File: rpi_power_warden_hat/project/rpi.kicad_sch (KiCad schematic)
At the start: 5 parts, among them J1 Conn_01x06, J4 Conn_01x06, J5 Raspberry_Pi_4

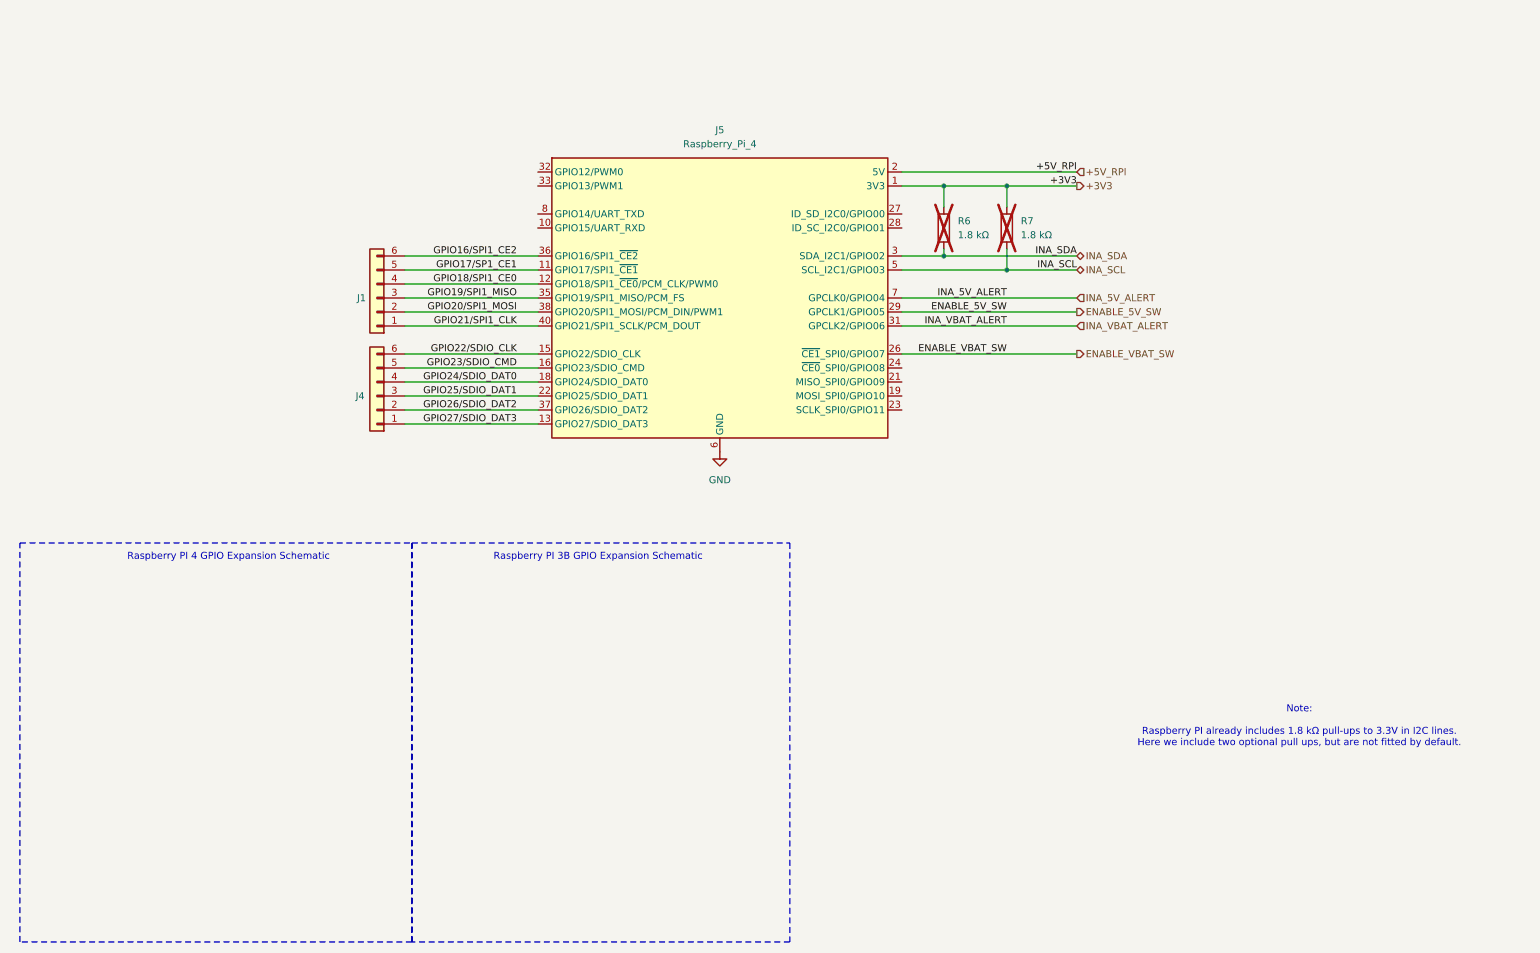
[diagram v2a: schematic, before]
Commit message: re-annotate schematic, add leds to power supply outputs and add connector for VBAT switched load
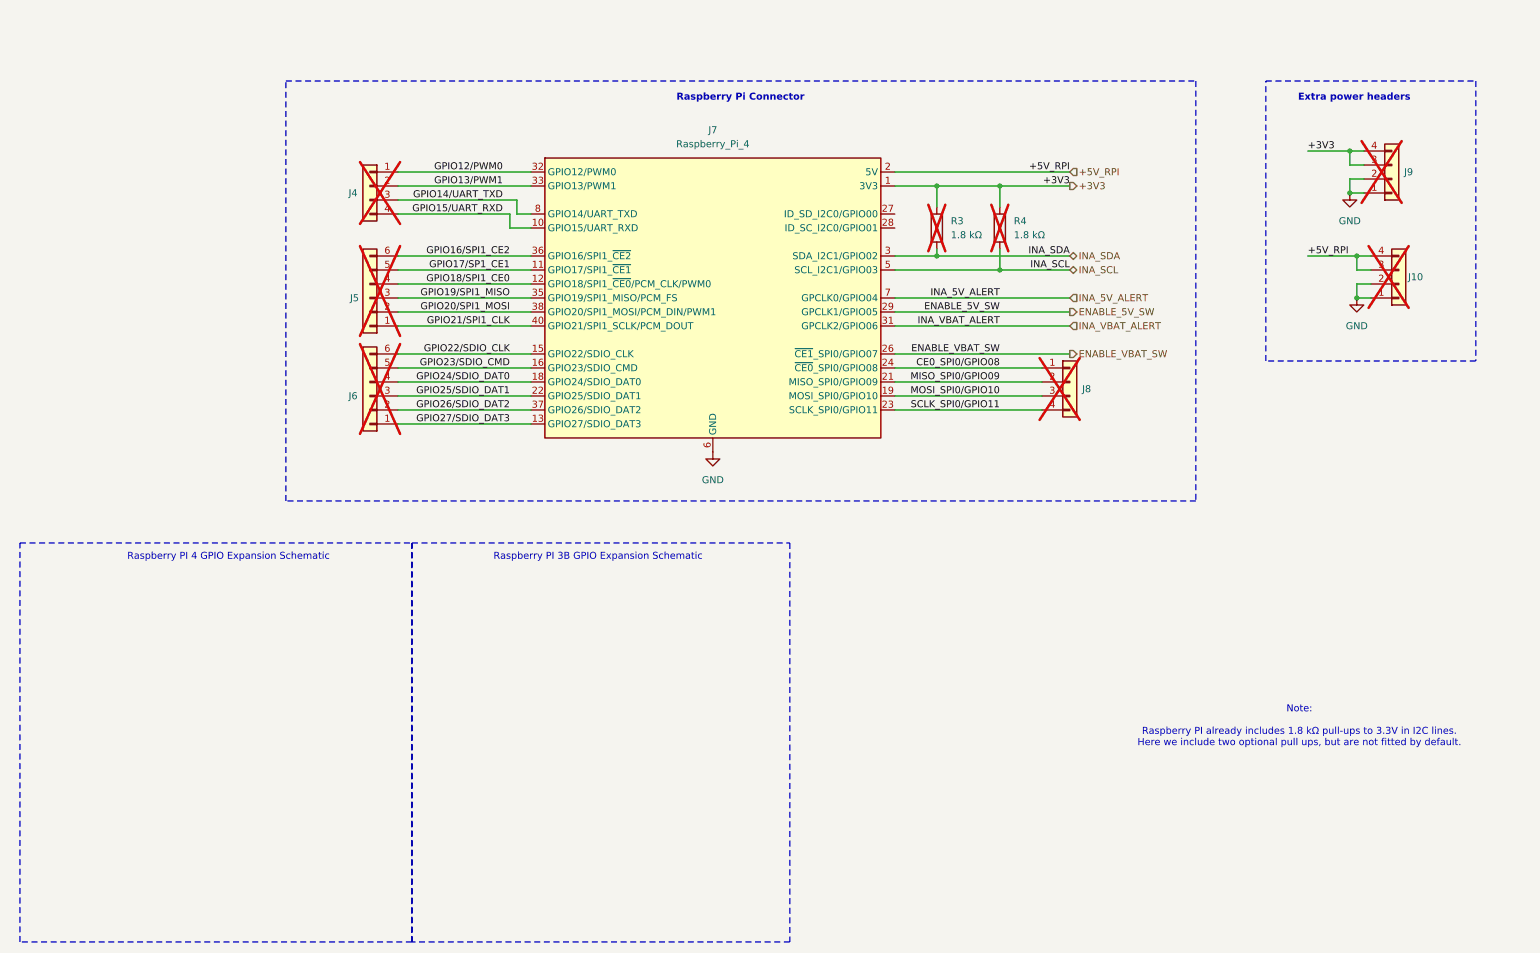
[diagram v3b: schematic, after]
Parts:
- added J10, J4, J8, J9: Conn_01x04, Connector_PinHeader_1.00mm:PinHeader_1x04_P1.00mm_Vertical, symbol Connector_Generic:Conn_01x04
- J5: renamed from J1; footprint (none) -> Connector_PinHeader_1.00mm:PinHeader_1x06_P1.00mm_Vertical; now not fitted; now left out of the parts list
- J6: renamed from J4; footprint (none) -> Connector_PinHeader_1.00mm:PinHeader_1x06_P1.00mm_Vertical; now not fitted; now left out of the parts list
- renumbered J5 to J7, R6 to R3, R7 to R4
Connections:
- net +3V3: now also J9.3 (Pin_3), J9.4 (Pin_4)
- net +5V_RPI: now also J10.3 (Pin_3), J10.4 (Pin_4)
- net GND: now also J10.1 (Pin_1), J10.2 (Pin_2), J9.1 (Pin_1), J9.2 (Pin_2)
- net GPIO15/UART_RXD: now reaches J7.10 (GPIO15/UART_RXD)
- net GPIO15/UART_RXD: now also J4.4 (Pin_4)
- net MOSI_SPI0/GPIO10: now reaches J7.19 (MOSI_SPI0/GPIO10)
- net MOSI_SPI0/GPIO10: now also J8.3 (Pin_3)
- net MISO_SPI0/GPIO09: now reaches J7.21 (MISO_SPI0/GPIO09)
- net MISO_SPI0/GPIO09: now also J8.2 (Pin_2)
- net SCLK_SPI0/GPIO11: now reaches J7.23 (SCLK_SPI0/GPIO11)
- net SCLK_SPI0/GPIO11: now also J8.4 (Pin_4)
- net CE0_SPI0/GPIO08: now reaches J7.24 (~{CE0}_SPI0/GPIO08)
- net CE0_SPI0/GPIO08: now also J8.1 (Pin_1)
- net GPIO12/PWM0: now reaches J7.32 (GPIO12/PWM0)
- net GPIO12/PWM0: now also J4.1 (Pin_1)
- net GPIO13/PWM1: now reaches J7.33 (GPIO13/PWM1)
- net GPIO13/PWM1: now also J4.2 (Pin_2)
- net GPIO14/UART_TXD: now reaches J7.8 (GPIO14/UART_TXD)
- net GPIO14/UART_TXD: now also J4.3 (Pin_3)
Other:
- note added: "Extra power headers"
- note added: "Raspberry Pi Connector"
- moved on the sheet: J7, R3, R4

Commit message: add RPi HAT eeprom to schematic
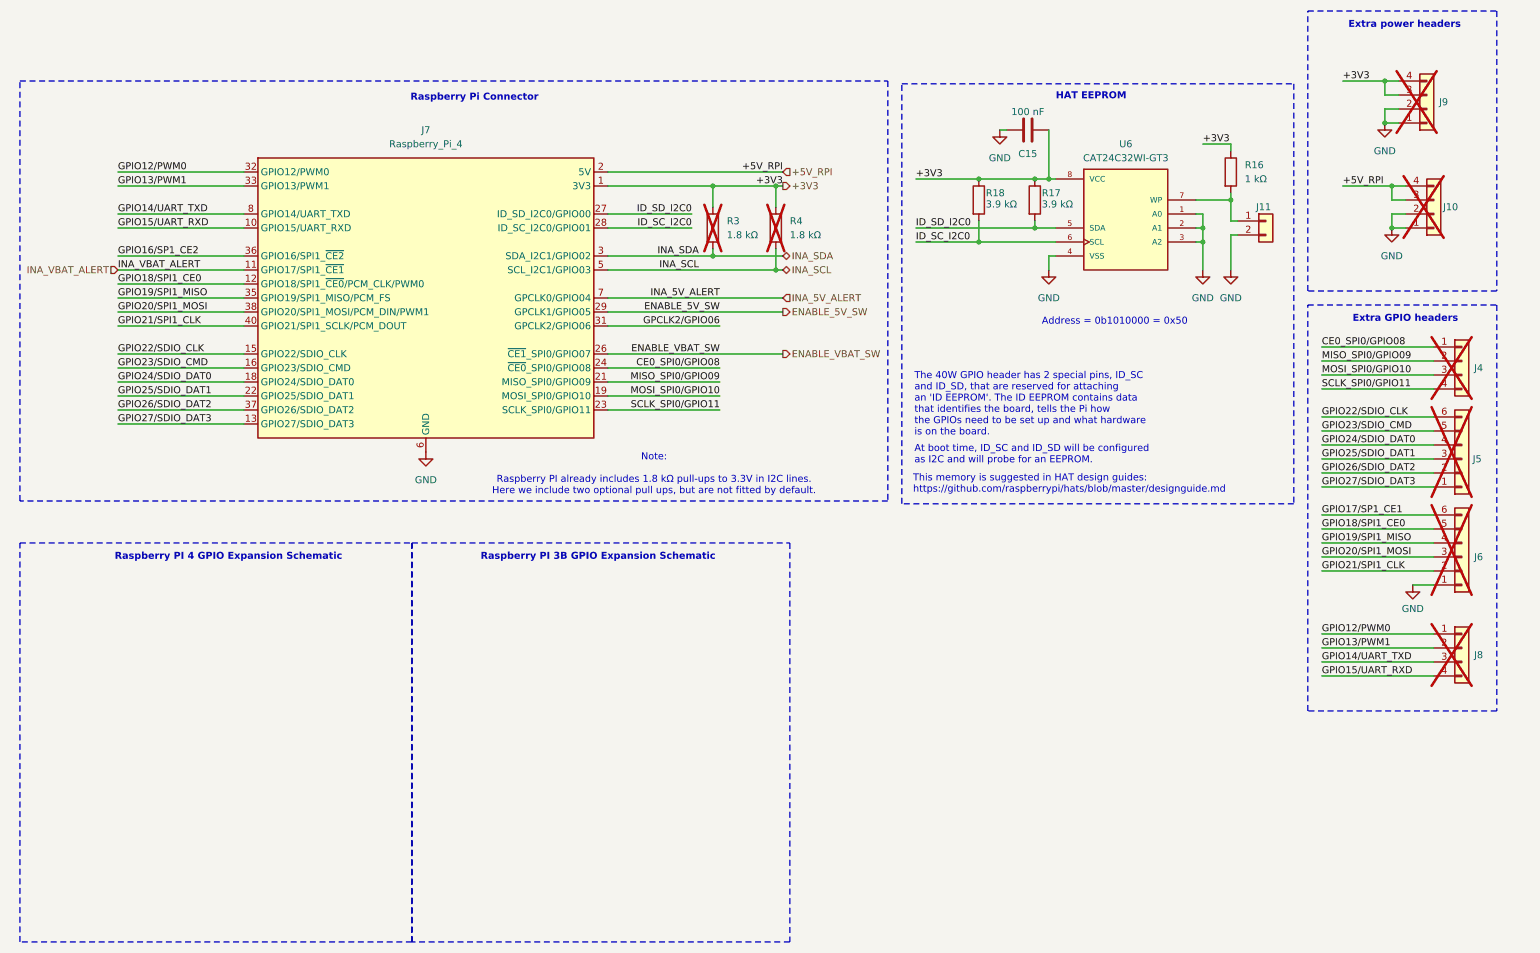
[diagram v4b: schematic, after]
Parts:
- added C15: 100 nF, Capacitor_SMD:C_0603_1608Metric_Pad1.08x0.95mm_HandSolder, symbol Device:C
- added J11: Conn_01x02, symbol Connector_Generic:Conn_01x02
- added R16: 1 kΩ, Resistor_SMD:R_0603_1608Metric_Pad0.98x0.95mm_HandSolder, symbol Device:R
- added R17, R18: 3.9 kΩ, Resistor_SMD:R_0603_1608Metric_Pad0.98x0.95mm_HandSolder, symbol Device:R
- added U6: CAT24C32WI-GT3, rpi_power_warden_hat:SOIC-8, symbol rpi_power_warden_hat:CAT24C32WI-GT3
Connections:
- net +3V3: now also C15.1, R16.1, R17.1, R18.1, U6.8 (VCC)
- net CE0_SPI0/GPIO08: now also J4.1 (Pin_1); no longer J8.1 (Pin_1)
- net GND: now also J6.1 (Pin_1), C15.2, J11.2 (Pin_2), U6.1 (A0), U6.2 (A1), U6.3 (A2), U6.4 (VSS)
- net GPIO12/PWM0: now also J8.1 (Pin_1); no longer J4.1 (Pin_1)
- net GPIO13/PWM1: now also J8.2 (Pin_2); no longer J4.2 (Pin_2)
- net GPIO14/UART_TXD: now also J8.3 (Pin_3); no longer J4.3 (Pin_3)
- net GPIO15/UART_RXD: now also J8.4 (Pin_4); no longer J4.4 (Pin_4)
- net GPIO17/SP1_CE1: now also J6.6 (Pin_6); no longer J5.5 (Pin_5), J7.11 (GPIO17/SPI1_~{CE1})
- net GPIO18/SPI1_CE0: now also J6.5 (Pin_5); no longer J5.4 (Pin_4)
- net GPIO19/SPI1_MISO: now also J6.4 (Pin_4); no longer J5.3 (Pin_3)
- net GPIO20/SPI1_MOSI: now also J6.3 (Pin_3); no longer J5.2 (Pin_2)
- net GPIO21/SPI1_CLK: now also J6.2 (Pin_2); no longer J5.1 (Pin_1)
- net GPIO22/SDIO_CLK: now also J5.6 (Pin_6); no longer J6.6 (Pin_6)
- net GPIO23/SDIO_CMD: now also J5.5 (Pin_5); no longer J6.5 (Pin_5)
- net GPIO24/SDIO_DAT0: now also J5.4 (Pin_4); no longer J6.4 (Pin_4)
- net GPIO25/SDIO_DAT1: now also J5.3 (Pin_3); no longer J6.3 (Pin_3)
- net GPIO26/SDIO_DAT2: now also J5.2 (Pin_2); no longer J6.2 (Pin_2)
- net GPIO27/SDIO_DAT3: now also J5.1 (Pin_1); no longer J6.1 (Pin_1)
- net INA_VBAT_ALERT: now also J7.11 (GPIO17/SPI1_~{CE1}); no longer J7.31 (GPCLK2/GPIO06)
- net MISO_SPI0/GPIO09: now also J4.2 (Pin_2); no longer J8.2 (Pin_2)
- net MOSI_SPI0/GPIO10: now also J4.3 (Pin_3); no longer J8.3 (Pin_3)
- net SCLK_SPI0/GPIO11: now also J4.4 (Pin_4); no longer J8.4 (Pin_4)
- net ID_SD_I2C0: now reaches J7.27 (ID_SD_I2C0/GPIO00)
- net ID_SD_I2C0: now also R17.2, U6.5 (SDA)
- net ID_SC_I2C0: now reaches J7.28 (ID_SC_I2C0/GPIO01)
- net ID_SC_I2C0: now also R18.2, U6.6 (SCL)
- net GPIO16/SPI1_CE2 renamed GPIO16/SP1_CE2
- net GPIO16/SP1_CE2: no longer J5.6 (Pin_6)
- new net: J11.1 (Pin_1), R16.2, U6.7 (WP)
- new net GPCLK2/GPIO06: J7.31 (GPCLK2/GPIO06)
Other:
- note added: "Address = 0b1010000 = 0x50"
- note added: "At boot time, ID_SC and ID_SD will be configured as I2C and will probe for an EEPROM."
- note added: "Extra GPIO headers"
- note added: "HAT EEPROM"
- note added: "The 40W GPIO header has 2 special pins, ID_SC and ID_SD, that are reserved for attaching an 'ID EEPROM'. The ID EEPROM contains data that identifies the board, tells the Pi how the GPIOs need to be set up and what hardware is on the board."
- note added: "This memory is suggested in HAT design guides: https://github.com/raspberrypi/hats/blob/master/designguide.md"
- moved on the sheet: J10, J7, J9, R3, R4

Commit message: add: raspberry pi footprint
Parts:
- J7: footprint Connector_PinSocket_2.54mm:PinSocket_2x20_P2.54mm_Vertical -> rpi_power_warden_hat:RPI_Hat_B+
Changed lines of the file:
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@@
 			)
 		)
-		(property "Footprint" "Connector_PinSocket_2.54mm:PinSocket_2x20_P2.54mm_Vertical"
+		(property "Footprint" "rpi_power_warden_hat:RPI_Hat_B+"
 			(at 159.004 124.968 0)
 			(effects

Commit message: re-annotate schematic
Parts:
- renumbered C15 to C3, J6 to J10, J8 to J11, J7 to J4, J11 to J5, J9 to J6, J10 to J7, J4 to J8, J5 to J9, R18 to R5, R17 to R6, R16 to R7, U6 to U3
